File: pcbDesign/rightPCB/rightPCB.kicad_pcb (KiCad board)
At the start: 4 copper layers, 58.5 x 90 mm, 12 parts, among them J1 Conn_01x07_Pin, SW5 TL, SW6 TR, SW7 PS

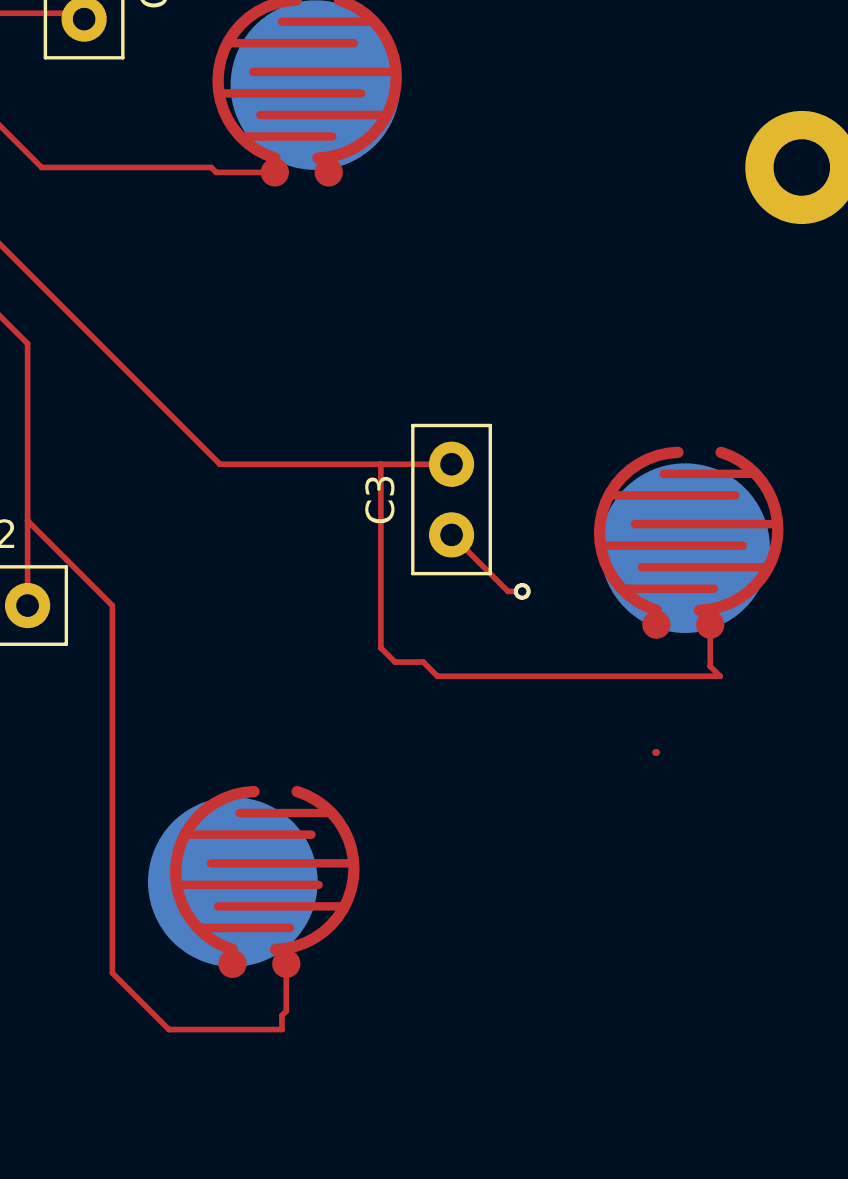
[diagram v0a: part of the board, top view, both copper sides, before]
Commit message: Updated pcbs and added footprint for rotary encoder (in progress)
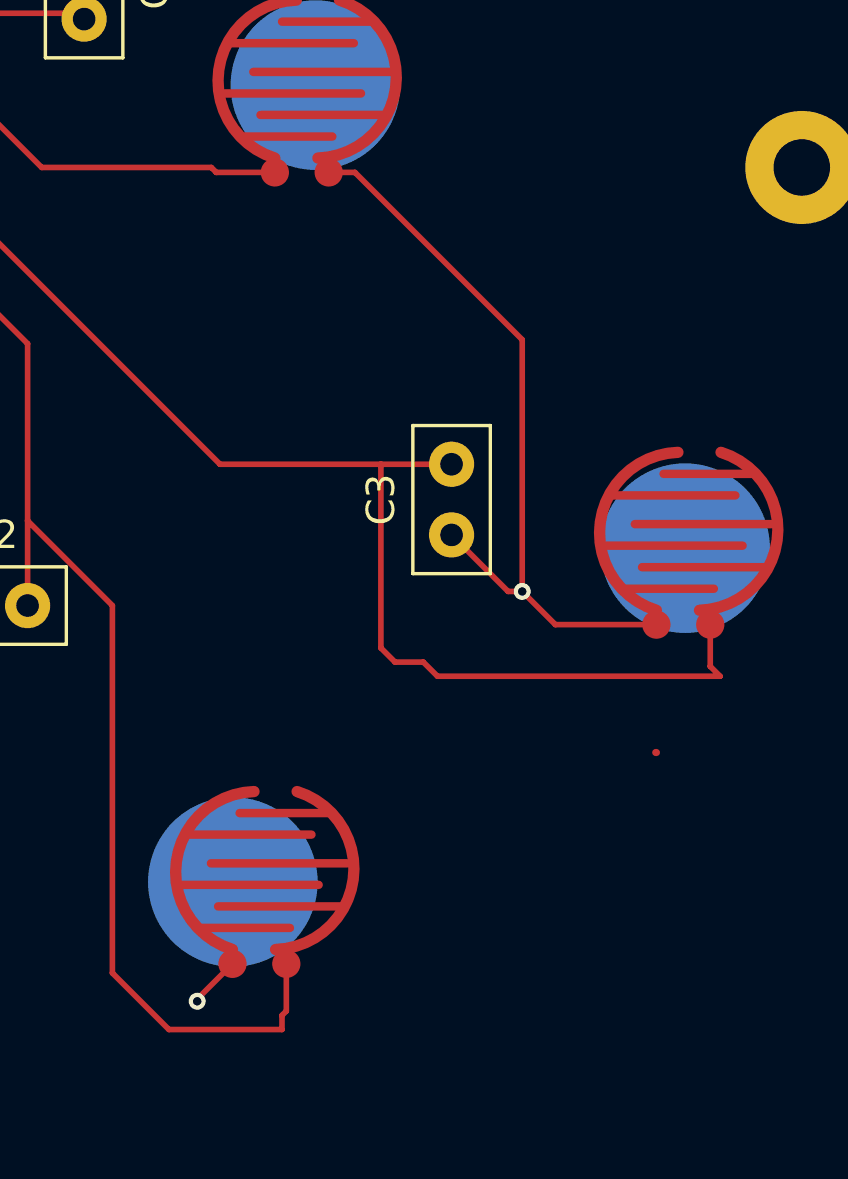
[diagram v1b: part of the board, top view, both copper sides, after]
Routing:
- net GND: track 22.4 -> 47.6 mm, vias 3 -> 4
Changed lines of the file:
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@@
+	)
+	(segment
+		(start 218.581453 79.1749)
+		(end 224.5 85.093447)
+		(width 0.2)
+		(layer "F.Cu")
+		(net 1)
 	)
 	(segment
@@
 		(end 229.22385 99.6986)
 		(width 0.254)
+		(layer "F.Cu")
+		(net 1)
+	)
+	(segment
+		(start 225.6741 95.1741)
+		(end 224.5 94)
+		(width 0.2)
 		(layer "F.Cu")
 		(net 1)
@@
 	)
 	(segment
+		(start 213 108.42435)
+		(end 213 108.5)
+		(width 0.2)
+		(layer "F.Cu")
+		(net 1)
+	)
+	(segment
 		(start 222 92)
 		(end 224 94)
+		(width 0.2)
+		(layer "F.Cu")
+		(net 1)
+	)
+	(segment
+		(start 224.5 85.093447)
+		(end 224.5 94)
+		(width 0.2)
+		(layer "F.Cu")
+		(net 1)
+	)
+	(segment
+		(start 229.24745 95.1741)
+		(end 225.6741 95.1741)
+		(width 0.2)
+		(layer "F.Cu")
+		(net 1)
+	)
+	(segment
+		(start 217.65335 79.1749)
+		(end 218.581453 79.1749)
 		(width 0.2)
 		(layer "F.Cu")
@@
 		(net 1)
 	)
+	(segment
+		(start 214.24875 107.1756)
+		(end 213 108.42435)
+		(width 0.2)
+		(layer "F.Cu")
+		(net 1)
+	)
 	(via
 		(at 224.5 94)
 		(size 0.6)
 		(drill 0.3)
+		(layers "F.Cu" "B.Cu")
+		(net 1)
+	)
+	(via
+		(at 213 108.5)
+		(size 0.6)
+		(drill 0.3)

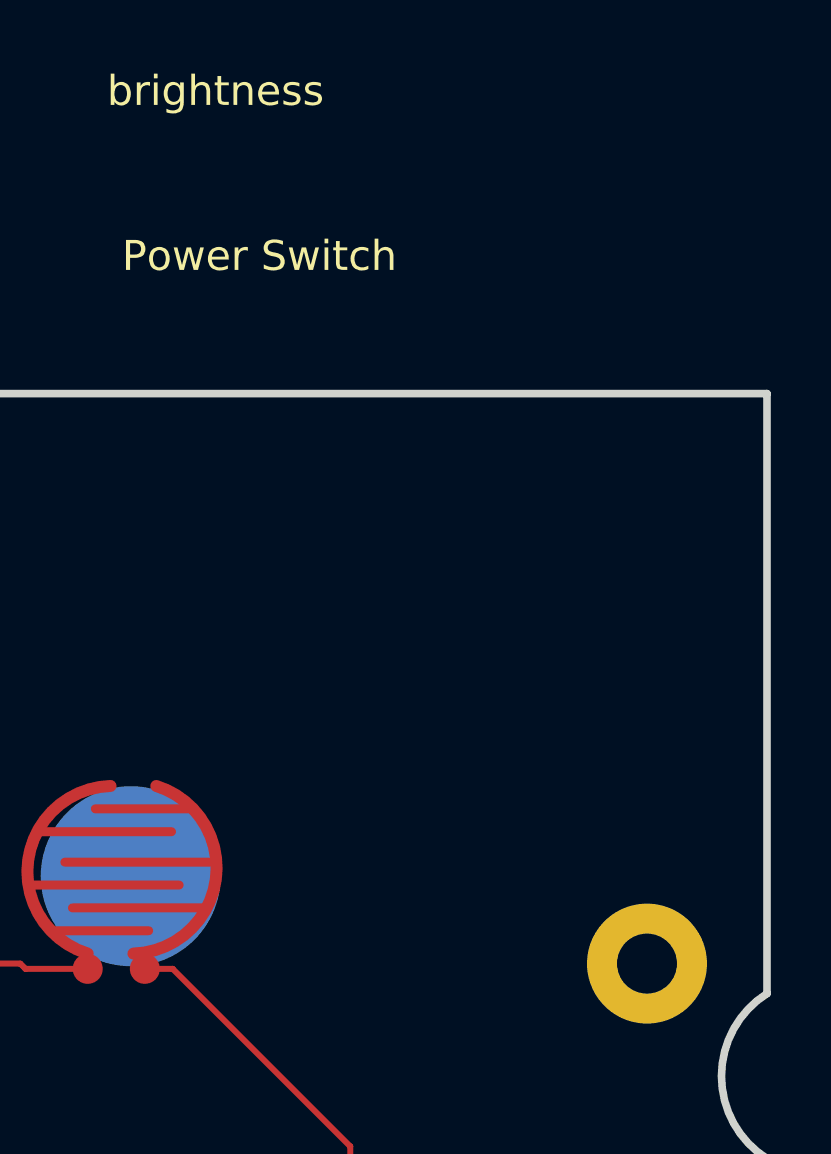
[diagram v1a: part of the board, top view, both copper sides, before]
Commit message: Updated PCB designs for left and right boards
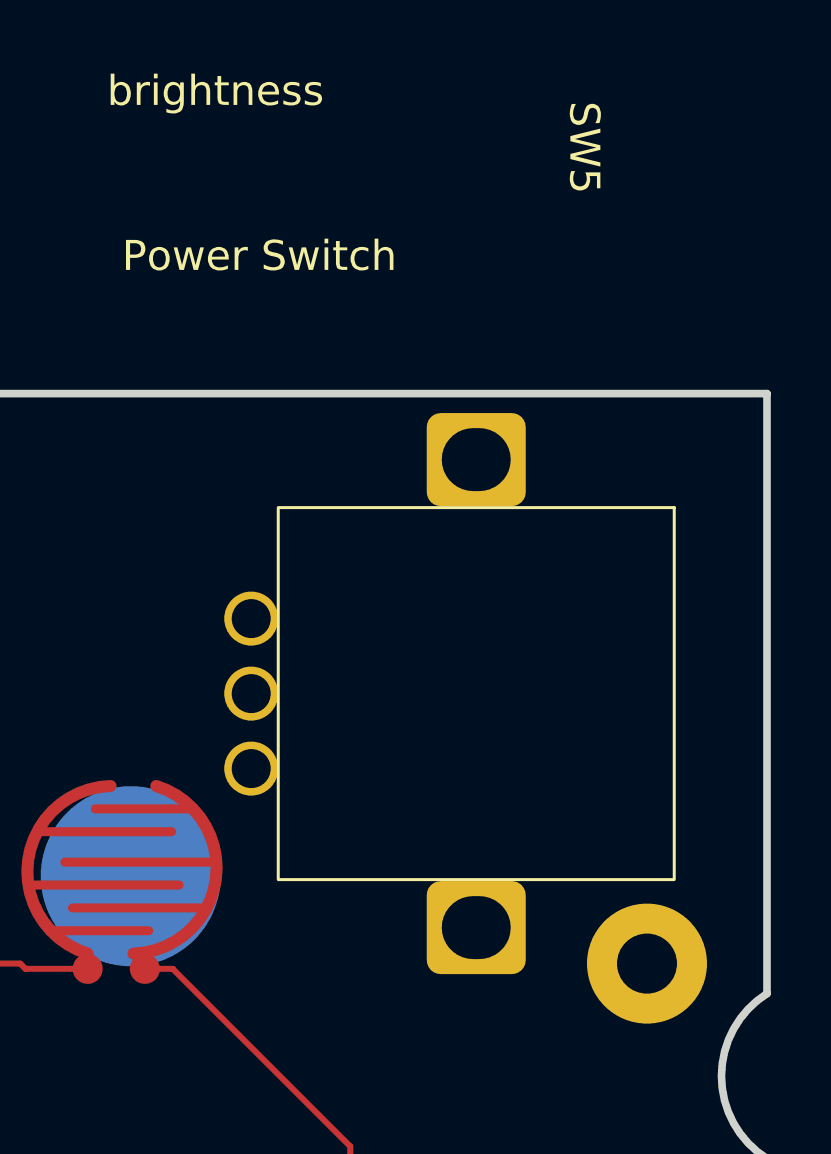
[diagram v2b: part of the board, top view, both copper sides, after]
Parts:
- added SW5: RotaryEncoder, GGLib:PES12, F.Cu at (235.3, 63.8)
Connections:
- J1 pad 3: /Start -> /1
- J1 pad 5: /1 -> /Start
- J1 pad 6: /Clk -> /Brightness_B
- J1 pad 7: /Brightness_DT -> /Brightness_A

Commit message: Routed
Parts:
- removed ?: , 
- removed Hole_gge24790: Hole_gge24790, BackupProjects_allisonbarfield_personal_3_20250219:Hole_gge24790
- removed Hole_gge24795: Hole_gge24795, BackupProjects_allisonbarfield_personal_3_20250219:Hole_gge24795
- added H1: MountingHole, MountingHole:MountingHole_2mm, F.Cu at (193.4, 63.0)
- added H2: MountingHole, MountingHole:MountingHole_2mm, F.Cu at (193.9, 115.5)
- added H3: MountingHole, MountingHole:MountingHole_3.5mm, F.Cu at (185.1, 126.0)
- moved SW8 1.20 mm to (217.2, 74.8)
- renumbered SW5 to SW6, SW6 to SW7, SW7 to SW8
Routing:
- net GND: track 47.6 -> 104.1 mm, vias 4 -> 0
- net /Brightness_A: track 0.00 -> 48.2 mm, vias 0 -> 1
- net /Brightness_B: track 0.00 -> 24.4 mm
- net /2: track 48.1 -> 55.3 mm
- net /Start: track 23.3 -> 19.5 mm
- added copper zone on In1.Cu, net GND

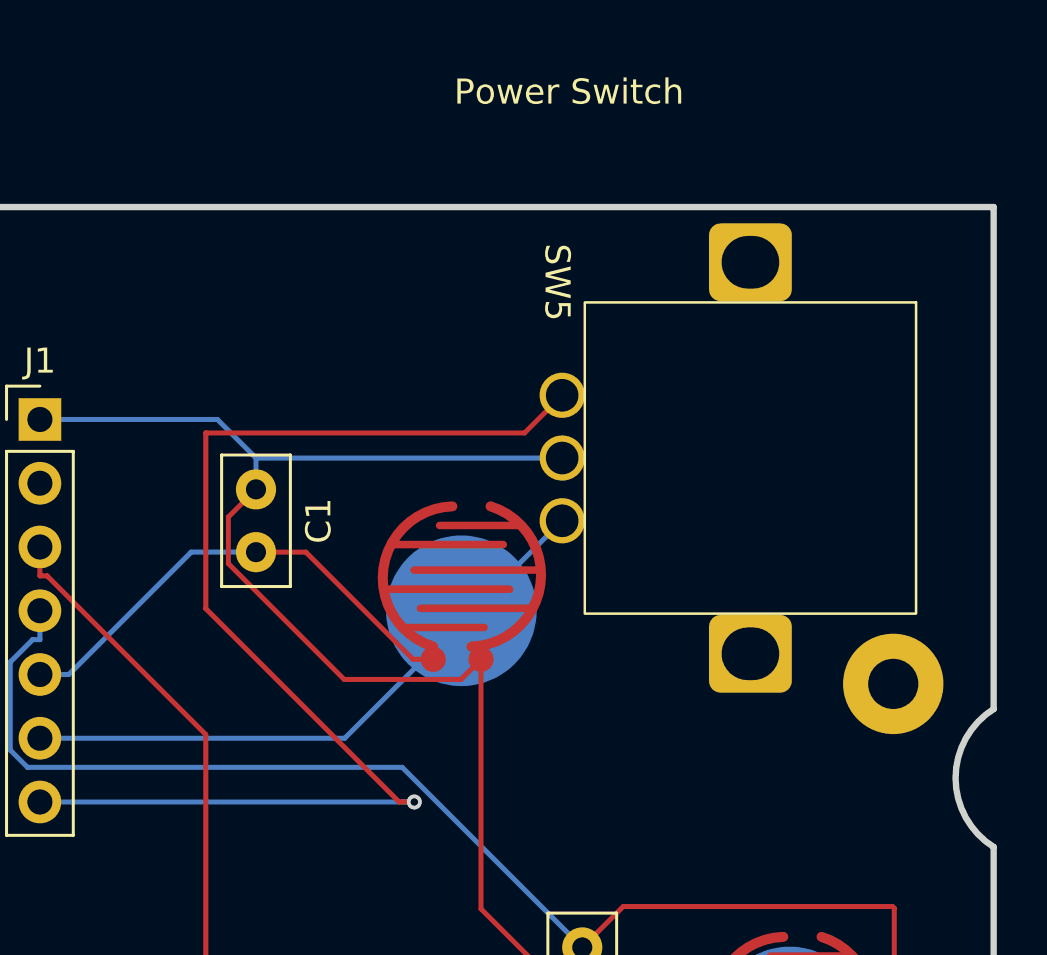
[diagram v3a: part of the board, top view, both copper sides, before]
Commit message: Edited PCB for rotary encoder
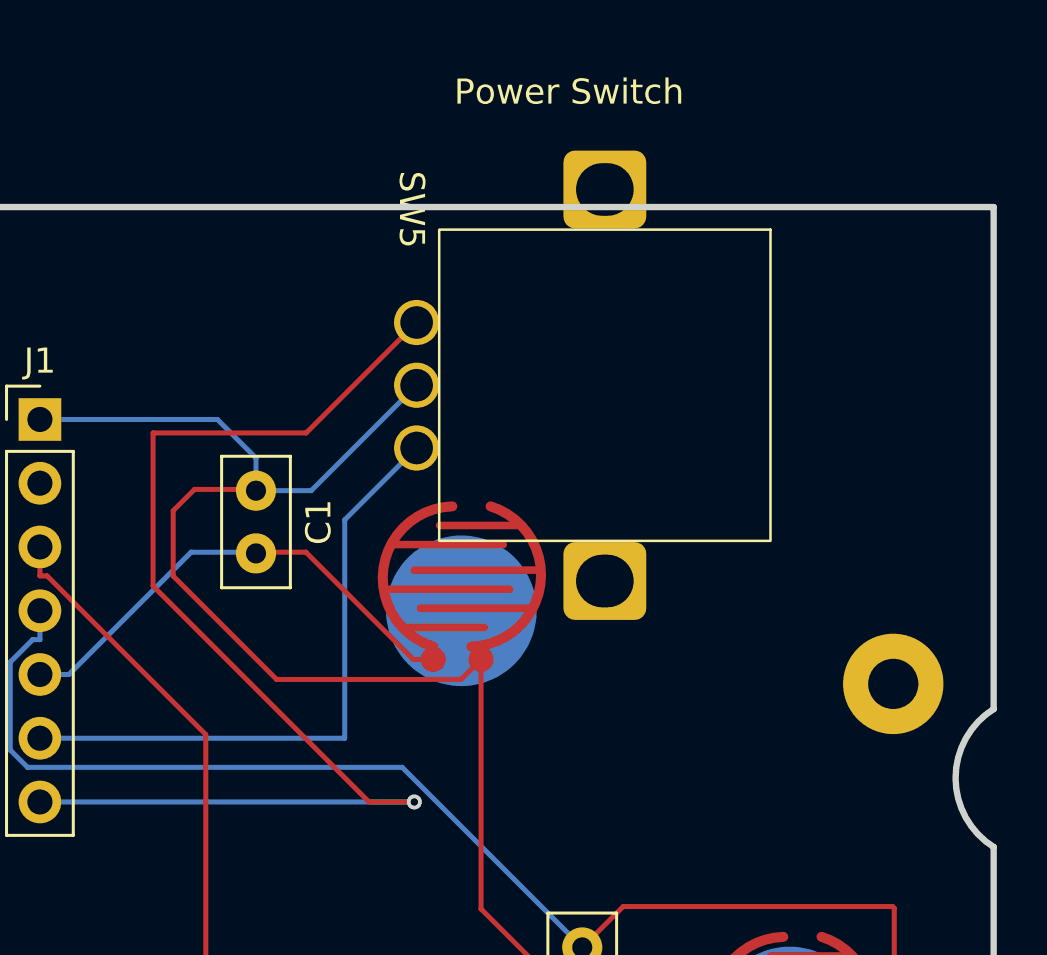
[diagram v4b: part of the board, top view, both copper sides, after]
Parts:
- moved SW5 6.48 mm to (229.5, 60.9)
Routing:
- net /Brightness_A: track 48.2 -> 47.3 mm
- net GND: track 104.1 -> 104.9 mm
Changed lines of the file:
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@@
 	(footprint "GGLib:PES12"
 		(layer "F.Cu")
-		(at 235.3 63.8 -90)
+		(at 229.5 60.9 -90)
 		(property "Reference" "SW5"
 			(at -0.8 14.3 270)
@@
 	(footprint "Capacitor_THT:C_Disc_D5.0mm_W2.5mm_P2.50mm"
 		(layer "F.Cu")
-		(at 209 71.25 -90)
+		(at 209 71.3 -90)
 		(descr "C, Disc series, Radial, pin pitch=2.50mm, , diameter*width=5*2.5mm^2, Capacitor, http://cdn-reichelt.de/documents/datenblatt/B300/DS_KERKO_TC.pdf")
 		(tags "C Disc series Radial pin pitch 2.50mm  diameter 5mm width 2.5mm Capacitor")
@@
 	)
 	(segment
+		(start 206.55 71.25)
+		(end 209 71.25)
+		(width 0.2)
+		(layer "F.Cu")
+		(net 1)
+	)
+	(segment
 		(start 222 95.1741)
 		(end 217.1947 95.1741)
@@
 	)
 	(segment
+		(start 205.7 72.1)
+		(end 206.55 71.25)
+		(width 0.2)
+		(layer "F.Cu")
+		(net 1)
+	)
+	(segment
 		(start 217.9658 87.9658)
 		(end 217.9658 78.0211)
@@
 	)
 	(segment
-		(start 212.51505 78.8221)
-		(end 207.899 74.20605)
-		(width 0.2)
-		(layer "F.Cu")
-		(net 1)
-	)
-	(segment
-		(start 207.899 72.351)
-		(end 209 71.25)
-		(width 0.2)
-		(layer "F.Cu")
-		(net 1)
-	)
-	(segment
 		(start 229.2475 95.1741)
 		(end 222 95.1741)
@@
 	)
 	(segment
+		(start 217.9658 78.0211)
+		(end 217.1648 78.8221)
+		(width 0.2)
+		(layer "F.Cu")
+		(net 1)
+	)
+	(segment
 		(start 211.1486 104.8771)
 		(end 213.4471 107.1756)
@@
 	)
 	(segment
+		(start 209.8221 78.8221)
+		(end 205.7 74.7)
+		(width 0.2)
+		(layer "F.Cu")
+		(net 1)
+	)
+	(segment
 		(start 217.1947 95.1741)
 		(end 211.1486 101.2202)
@@
 	)
 	(segment
-		(start 207.899 74.20605)
-		(end 207.899 72.351)
+		(start 217.1648 78.8221)
+		(end 209.8221 78.8221)
 		(width 0.2)
 		(layer "F.Cu")
@@
 	)
 	(segment
-		(start 217.1648 78.8221)
-		(end 212.51505 78.8221)
-		(width 0.2)
-		(layer "F.Cu")
-		(net 1)
-	)
-	(segment
-		(start 217.9658 78.0211)
-		(end 217.1648 78.8221)
+		(start 205.7 74.7)
+		(end 205.7 72.1)
 		(width 0.2)
 		(layer "F.Cu")
@@
 	)
 	(segment
+		(start 211.2 71.3)
+		(end 215.4 67.1)
+		(width 0.2)
+		(layer "B.Cu")
+		(net 1)
+	)
+	(segment
 		(start 207.4641 68.4641)
 		(end 200.3906 68.4641)
@@
 	)
 	(segment
-		(start 209 70)
-		(end 221.2 70)
+		(start 209 71.3)
+		(end 211.2 71.3)
 		(width 0.2)
 		(layer "B.Cu")
@@
 	)
 	(segment
-		(start 207 69)
-		(end 219.7 69)
+		(start 213.5041 83.7041)
+		(end 204.9 75.1)
 		(width 0.2)
 		(layer "F.Cu")
@@
 	)
 	(segment
-		(start 207 76)
-		(end 207 69)
+		(start 211 69)
+		(end 215.4 64.6)
 		(width 0.2)
 		(layer "F.Cu")
@@
 	)
 	(segment
+		(start 204.9 75.1)
+		(end 204.9 69)
+		(width 0.2)
+		(layer "F.Cu")
+		(net 6)
+	)
+	(segment
 		(start 215.3076 83.7041)
-		(end 214.7041 83.7041)
+		(end 213.5041 83.7041)
 		(width 0.2)
 		(layer "F.Cu")
@@
 	)
 	(segment
-		(start 214.7041 83.7041)
-		(end 207 76)
-		(width 0.2)
-		(layer "F.Cu")
-		(net 6)
-	)
-	(segment
-		(start 219.7 69)
-		(end 221.2 67.5)
+		(start 204.9 69)
+		(end 211 69)
 		(width 0.2)
 		(layer "F.Cu")
@@
 	(segment
 		(start 212.5359 81.1641)
-		(end 221.2 72.5)
-		(width 0.2)
-		(layer "B.Cu")
+		(end 212.5359 72.4641)
+		(width 0.2)
+		(layer "B.Cu")
+		(net 7)
+	)
+	(segment
+		(start 212.5359 72.4641)
+		(end 215.4 69.6)
+		(width 0.2)
+		(layer "B.Cu")
